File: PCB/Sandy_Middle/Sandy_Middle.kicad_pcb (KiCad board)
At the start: 2 copper layers, 285 x 73.4 mm, 62 parts, among them J1 Conn_02x02_Top_Bottom, J2 Conn_02x02_Top_Bottom, J3 Conn_02x02_Top_Bottom

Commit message: WIP ネジ穴位置、スイッチ位置調整中
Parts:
- removed EXT_MC7: Conn_01x01, TestPoint:TestPoint_THTPad_D2.0mm_Drill1.0mm
- added H20: MountingHole, locallib:MountingHole_2.2mm_M2_Pad_minimal, F.Cu at (41.3, 13.9)
- added H21: MountingHole, locallib:MountingHole_2.2mm_M2_Pad_minimal, F.Cu at (47.3, 13.9)
- SW_BS1: renamed from SW_BS1.5u1; footprint MX_Alps_Hybrid:MXOnly-1.5U-Hotswap-guide -> MX_Alps_Hybrid:MXOnly-1U-Hotswap-guide
- SW_TAB1: renamed from SW_TAB1.5u1; footprint MX_Alps_Hybrid:MXOnly-1.5U-Hotswap-guide -> MX_Alps_Hybrid:MXOnly-1U-Hotswap-guide
- moved D6 7.24 mm to (287.8, 42.5)
- moved SW_TAB1 4.76 mm to (40.1, 49.6)
- moved SW_BS1 4.76 mm to (287.8, 49.6), turned to 180 degrees
- renumbered SW_R4CenterC1 to SW_R4CNT_C1, SW_R4CenterL1 to SW_R4CNT_L1, SW_R4CenterR1 to SW_R4CNT_R1
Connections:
- D11 pad 1: Mid_row3 -> Mid_row8
- D12 pad 1: Mid_row8 -> Mid_row3
- J2 pad 4: Mid_col7 -> unconnected-(J2-Pin_4-Pad4)_1
- SW_R4CNT_L1 pad 1: Mid_col3 -> Mid_col2
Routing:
- net Mid_row6: track 289.5 -> 0.00 mm, vias 3 -> 0
- net Mid_row1: track 281.4 -> 0.00 mm, vias 3 -> 0
- net Mid_col0: track 201.1 -> 0.00 mm, vias 3 -> 0
- net Mid_col6: track 139.1 -> 0.00 mm, vias 3 -> 0
- net Mid_col3: track 137.7 -> 0.00 mm, vias 3 -> 0
- net Mid_row7: track 131.6 -> 0.00 mm, vias 5 -> 0
- net Mid_row2: track 120.4 -> 0.00 mm, vias 4 -> 0
- net Mid_row3: track 110.2 -> 0.00 mm, vias 1 -> 0
- net Mid_col4: track 94.5 -> 0.00 mm, vias 5 -> 0
- net Mid_row8: track 86.1 -> 0.00 mm, vias 1 -> 0
- net Mid_col2: track 69.1 -> 0.00 mm, vias 2 -> 0
- net Mid_col7: track 40.0 -> 0.00 mm, vias 1 -> 0
- net Net-(D8-A): track 22.1 -> 0.00 mm
- net Net-(D9-A): track 11.4 -> 0.00 mm
- net Net-(D7-A): track 9.12 -> 0.00 mm
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
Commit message: Mid→Topのネジ穴を追加して配置
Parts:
- added ?: , clipboard:1d23b097-72e0-487b-bec7-a328ee8b6ed7, F.Cu at (144.8, -0.45)
- added D1: D, locallib:D_SOD-123_Emphasized_Direction_Line, B.Cu at (41.3, -20.7)
- added D10: D, locallib:D_SOD-123_Emphasized_Direction_Line, B.Cu at (212.8, -19.6)
- added D11: D, locallib:D_SOD-123_Emphasized_Direction_Line, B.Cu at (231.8, -20.7)
- added D12: D, locallib:D_SOD-123_Emphasized_Direction_Line, B.Cu at (250.9, -19.6)
- added D13: D, locallib:D_SOD-123_Emphasized_Direction_Line, B.Cu at (269.9, -20.7)
- added D14: D, locallib:D_SOD-123_Emphasized_Direction_Line, B.Cu at (289.0, -19.6)
- added D16: D, locallib:D_SOD-123_Emphasized_Direction_Line, B.Cu at (141.3, -5.21)
- added D17: D, locallib:D_SOD-123_Emphasized_Direction_Line, B.Cu at (160.4, -5.21)
- added D18: D, locallib:D_SOD-123_Emphasized_Direction_Line, B.Cu at (174.7, -1.64)
- added D19: D, locallib:D_SOD-123_Emphasized_Direction_Line, B.Cu at (179.4, -5.21)
- added D2: D, locallib:D_SOD-123_Emphasized_Direction_Line, B.Cu at (60.4, -19.6)
- added D3: D, locallib:D_SOD-123_Emphasized_Direction_Line, B.Cu at (79.4, -20.7)
- added D4: D, locallib:D_SOD-123_Emphasized_Direction_Line, B.Cu at (98.5, -19.6)
- added D5: D, locallib:D_SOD-123_Emphasized_Direction_Line, B.Cu at (117.5, -20.7)
- added D6: D, locallib:D_SOD-123_Emphasized_Direction_Line, B.Cu at (136.6, -19.6)
- added D7: D, locallib:D_SOD-123_Emphasized_Direction_Line, B.Cu at (193.7, -20.7)
- added D8: D, locallib:D_SOD-123_Emphasized_Direction_Line, B.Cu at (155.6, -20.8)
- added D9: D, locallib:D_SOD-123_Emphasized_Direction_Line, B.Cu at (174.7, -20.7)
- added EXT_TC0: Conn_01x01, TestPoint:TestPoint_THTPad_D2.0mm_Drill1.0mm, B.Cu at (37.8, -30.2)
- added EXT_TC1: Conn_01x01, TestPoint:TestPoint_THTPad_D2.0mm_Drill1.0mm, B.Cu at (75.9, -30.2)
- added EXT_TC2: Conn_01x01, TestPoint:TestPoint_THTPad_D2.0mm_Drill1.0mm, B.Cu at (94.9, -30.2)
- added EXT_TC3: Conn_01x01, TestPoint:TestPoint_THTPad_D2.0mm_Drill1.0mm, B.Cu at (152.1, -30.2)
- added EXT_TC4: Conn_01x01, TestPoint:TestPoint_THTPad_D2.0mm_Drill1.0mm, B.Cu at (171.1, -30.3)
- added EXT_TC5: Conn_01x01, TestPoint:TestPoint_THTPad_D2.0mm_Drill1.0mm, B.Cu at (228.3, -30.2)
- added EXT_TC6: Conn_01x01, TestPoint:TestPoint_THTPad_D2.0mm_Drill1.0mm, B.Cu at (266.4, -30.2)
- added EXT_TR0: Conn_01x01, TestPoint:TestPoint_THTPad_D2.0mm_Drill1.0mm, B.Cu at (42.5, -18.3)
- added EXT_TR1: Conn_01x01, TestPoint:TestPoint_THTPad_D2.0mm_Drill1.0mm, B.Cu at (153.3, -14.7)
- added EXT_TR5: Conn_01x01, TestPoint:TestPoint_THTPad_D2.0mm_Drill1.0mm, B.Cu at (46.1, -18.3)
- added EXT_TR6: Conn_01x01, TestPoint:TestPoint_THTPad_D2.0mm_Drill1.0mm, B.Cu at (149.7, -14.7)
- added H1: MountingHole, locallib:MountingHole_2.2mm_M2_Pad_minimal, B.Cu at (28.2, -30.7)
- added H10: MountingHole, locallib:MountingHole_2.2mm_M2_Pad_minimal, B.Cu at (294.9, -18.3)
- added H11: MountingHole, locallib:MountingHole_2.2mm_M2_Pad_minimal, B.Cu at (142.5, 0.74)
- added H12: MountingHole, locallib:MountingHole_2.2mm_M2_Pad_minimal, B.Cu at (180.6, 0.74)
- added H2: MountingHole, locallib:MountingHole_2.2mm_M2_Pad_minimal, B.Cu at (123.5, -30.7)
- added H3: MountingHole, locallib:MountingHole_2.2mm_M2_Pad_minimal, B.Cu at (199.7, -30.7)
- added H4: MountingHole, locallib:MountingHole_2.2mm_M2_Pad_minimal, B.Cu at (294.9, -30.7)
- added H5: MountingHole, locallib:MountingHole_2.2mm_M2_Pad_minimal, B.Cu at (28.2, -18.3)
- added H6: MountingHole, locallib:MountingHole_2.2mm_M2_Pad_minimal, B.Cu at (66.3, -23.1)
- added H7: MountingHole, locallib:MountingHole_2.2mm_M2_Pad_minimal, B.Cu at (104.4, -23.1)
- added H8: MountingHole, locallib:MountingHole_2.2mm_M2_Pad_minimal, B.Cu at (218.7, -23.1)
- added H9: MountingHole, locallib:MountingHole_2.2mm_M2_Pad_minimal, B.Cu at (256.8, -23.1)
- added H_top_11: MountingHole, locallib:MountingHole_2.2mm_M2_Pad_minimal, B.Cu at (144.9, 55.6)
- added H_top_12: MountingHole, locallib:MountingHole_2.2mm_M2_Pad_minimal, B.Cu at (183.0, 55.6)
- added J1: Conn_02x02_Top_Bottom, locallib:JST_SH_SM04B-SRSS-TB_1x04-1MP_P1.00mm_Horizontal_wCable_housing_spare_pin, B.Cu at (171.1, -20.7)
- added J2: Conn_02x02_Top_Bottom, locallib:JST_SH_SM04B-SRSS-TB_1x04-1MP_P1.00mm_Horizontal_wCable_housing_spare_pin, B.Cu at (152.1, -20.7)
- added J3: Conn_02x02_Top_Bottom, locallib:JST_SH_SM04B-SRSS-TB_1x04-1MP_P1.00mm_Horizontal_wCable_housing_spare_pin, B.Cu at (135.4, -18.3)
- added REF**: 60_Outline, locallib:60_Outline-Sandy-Top2, F.Cu at (161.6, -14.7)
- added SW_-1: SW_Push, MX_Alps_Hybrid:MXOnly-1U-Hotswap-guide, F.Cu at (152.1, -24.3)
- added SW_1: SW_Push, MX_Alps_Hybrid:MXOnly-1U-Hotswap-guide, F.Cu at (56.8, -24.3)
- added SW_10: SW_Push, MX_Alps_Hybrid:MXOnly-1U-Hotswap-guide, F.Cu at (266.4, -24.3)
- added SW_2: SW_Push, MX_Alps_Hybrid:MXOnly-1U-Hotswap-guide, F.Cu at (75.9, -24.3)
- added SW_3: SW_Push, MX_Alps_Hybrid:MXOnly-1U-Hotswap-guide, F.Cu at (94.9, -24.3)
- added SW_4: SW_Push, MX_Alps_Hybrid:MXOnly-1U-Hotswap-screw-hole-side1-guide, F.Cu at (114.0, -24.3)
- added SW_5: SW_Push, MX_Alps_Hybrid:MXOnly-1U-Hotswap-guide, F.Cu at (133.0, -24.3)
- added SW_6: SW_Push, MX_Alps_Hybrid:MXOnly-1U-Hotswap-screw-hole-side1-guide, F.Cu at (190.2, -24.3)
- added SW_7: SW_Push, MX_Alps_Hybrid:MXOnly-1U-Hotswap-guide, F.Cu at (209.2, -24.3)
- added SW_8: SW_Push, MX_Alps_Hybrid:MXOnly-1U-Hotswap-guide, F.Cu at (228.3, -24.3)
- added SW_9: SW_Push, MX_Alps_Hybrid:MXOnly-1U-Hotswap-guide, F.Cu at (247.3, -24.3)
- added SW_=1: SW_Push, MX_Alps_Hybrid:MXOnly-1U-Hotswap-guide, F.Cu at (171.0, -24.3)
- added SW_ESC1: SW_Push, MX_Alps_Hybrid:MXOnly-1U-Hotswap-guide, F.Cu at (37.8, -24.3)
- added SW_INS1: SW_Push, MX_Alps_Hybrid:MXOnly-1U-Hotswap-screw-hole-side1-guide, F.Cu at (285.4, -24.3)
- added SW_T1: SW_Push, MX_Alps_Hybrid:MXOnly-1U-Hotswap-guide, F.Cu at (133.0, -5.21)
- added SW_Y1: SW_Push, MX_Alps_Hybrid:MXOnly-1U-Hotswap-guide, F.Cu at (190.2, -5.21)
- added SW_[1: SW_Push, MX_Alps_Hybrid:MXOnly-1U-Hotswap-guide, F.Cu at (152.1, -5.21)
- added SW_]1: SW_Push, MX_Alps_Hybrid:MXOnly-1U-Hotswap-guide, F.Cu at (171.1, -5.21)
- H_top_10: renamed from H21; moved to B.Cu
- H_top_4: renamed from H20; moved to B.Cu
- moved H_top_4 256.2 mm to (297.3, 24.1)
- moved H_top_10 251.1 mm to (297.3, 36.5), turned to 180 degrees
- moved H_top_7 181.0 mm to (106.8, 31.8)
- moved H_top_6 161.9 mm to (68.7, 31.8)
- moved H_top_8 79.8 mm to (221.1, 31.8)
- moved H_top_9 79.8 mm to (259.2, 31.8)
- moved H_top_5 66.8 mm to (30.6, 36.5)
- moved H_top_1 12.2 mm to (30.6, 24.1), turned to 0 degrees
- moved H_top_3 9.53 mm to (202.0, 24.1)
- moved H_top_2 9.52 mm to (125.8, 24.1)
- renumbered H14 to H_top_1, H12 to H_top_2, H13 to H_top_3, H15 to H_top_5, H16 to H_top_6, H17 to H_top_7, H18 to H_top_8, H19 to H_top_9
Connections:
- H1 pad 1: Mid_GND -> unconnected-(H1-Pad1)
- H10 pad 1: Mid_GND -> unconnected-(H10-Pad1)
- H11 pad 1: Mid_GND -> unconnected-(H11-Pad1)
- H2 pad 1: Mid_GND -> unconnected-(H2-Pad1)
- H3 pad 1: Mid_GND -> unconnected-(H3-Pad1)
- H4 pad 1: Mid_GND -> unconnected-(H4-Pad1)
- H5 pad 1: Mid_GND -> unconnected-(H5-Pad1)
- H6 pad 1: Mid_GND -> unconnected-(H6-Pad1)
- H7 pad 1: Mid_GND -> unconnected-(H7-Pad1)
- H8 pad 1: Mid_GND -> unconnected-(H8-Pad1)
- H9 pad 1: Mid_GND -> unconnected-(H9-Pad1)
- H_top_1 pad 1: Mid_GND -> unconnected-(H_top_1-Pad1)
- H_top_10 pad 1: Mid_GND -> unconnected-(H_top_10-Pad1)
- H_top_2 pad 1: Mid_GND -> unconnected-(H_top_2-Pad1)
- H_top_3 pad 1: Mid_GND -> unconnected-(H_top_3-Pad1)
- H_top_4 pad 1: Mid_GND -> unconnected-(H_top_4-Pad1)
- H_top_5 pad 1: Mid_GND -> unconnected-(H_top_5-Pad1)
- H_top_6 pad 1: Mid_GND -> unconnected-(H_top_6-Pad1)
- H_top_7 pad 1: Mid_GND -> unconnected-(H_top_7-Pad1)
- H_top_8 pad 1: Mid_GND -> unconnected-(H_top_8-Pad1)
- H_top_9 pad 1: Mid_GND -> unconnected-(H_top_9-Pad1)
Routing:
- added copper zone on B.Cu, net unconnected-(H5-Pad1)
- added copper zone on F.Cu, net unconnected-(H5-Pad1)
- removed copper zone on B.Cu, net Mid_GND
- removed copper zone on F.Cu, net Mid_GND
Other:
- board text added: "#Sandy_kbd v.0.2, Top by @jpskenn"
- board text added: "Top 1"
- board text added: "Top 2"
- board text added: "Top 3"
- board text added: "to Mid"

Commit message: Mid→Baseのネジ穴を追加して配置
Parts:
- removed ?: , clipboard:1d23b097-72e0-487b-bec7-a328ee8b6ed7
- removed the D1 at (41.3, -20.7)
- removed the D10 at (212.8, -19.6)
- removed the D11 at (231.8, -20.7)
- removed the D12 at (250.9, -19.6)
- removed the D13 at (269.9, -20.7)
- removed D14, D16, D17, D18, D19: D, locallib:D_SOD-123_Emphasized_Direction_Line
- removed the D2 at (60.4, -19.6)
- removed the D3 at (79.4, -20.7)
- removed the D4 at (98.5, -19.6)
- removed the D5 at (117.5, -20.7)
- removed the D6 at (136.6, -19.6)
- removed the D7 at (193.7, -20.7)
- removed the D8 at (155.6, -20.8)
- removed the D9 at (174.7, -20.7)
- removed EXT_TC0, EXT_TC1, EXT_TC2, EXT_TC3, EXT_TC4, EXT_TC5, EXT_TC6, EXT_TR0, EXT_TR1, EXT_TR5, EXT_TR6: Conn_01x01, TestPoint:TestPoint_THTPad_D2.0mm_Drill1.0mm
- removed the H1 at (28.2, -30.7)
- removed the H11 at (142.5, 0.74)
- removed the H12 at (180.6, 0.74)
- removed the H3 at (199.7, -30.7)
- removed the H4 at (294.9, -30.7)
- removed the H7 at (104.4, -23.1)
- removed the H8 at (218.7, -23.1)
- removed the J1 at (171.1, -20.7)
- removed the J2 at (152.1, -20.7)
- removed the J3 at (135.4, -18.3)
- removed the REF** at (161.6, -14.7)
- removed SW_-1, SW_1, SW_10, SW_2, SW_3, SW_5, SW_7, SW_8, SW_9, SW_=1, SW_ESC1, SW_T1, SW_Y1, SW_[1, SW_]1: SW_Push, MX_Alps_Hybrid:MXOnly-1U-Hotswap-guide
- removed SW_4, SW_6, SW_INS1: SW_Push, MX_Alps_Hybrid:MXOnly-1U-Hotswap-screw-hole-side1-guide
- H10, H2, H5, H6, H9: moved to F.Cu
- moved H6 241.6 mm to (303.2, 24.1)
- moved H5 225.5 mm to (249.7, 24.1)
- moved H9 201.5 mm to (65.1, 39.1), turned to 0 degrees
- moved H8 73.7 mm to (230.6, 36.5), turned to 0 degrees
- moved H2 71.5 mm to (78.2, 24.6), turned to 180 degrees
- moved H10 65.8 mm to (262.8, 39.1), turned to 0 degrees
- moved H4 57.7 mm to (192.5, 24.1), turned to 180 degrees
- moved H3 28.6 mm to (135.4, 24.1)
- moved H7 19.6 mm to (97.3, 36.5)
- renumbered H6 to H11, H7 to H12, H8 to H13, H9 to H14, H10 to H15, H11 to H16, H2 to H7, H5 to H8
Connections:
- H10 pad 1: (no net) -> unconnected-(H10-Pad1)
- H2 pad 1: (no net) -> unconnected-(H2-Pad1)
- H5 pad 1: (no net) -> unconnected-(H5-Pad1)
- H6 pad 1: (no net) -> unconnected-(H6-Pad1)
- H9 pad 1: (no net) -> unconnected-(H9-Pad1)
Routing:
- added copper zone on B.Cu, net unconnected-(H5-Pad1)
- added copper zone on F.Cu, net unconnected-(H5-Pad1)
- removed copper zone on B.Cu, net unconnected-(H8-Pad1)
- removed copper zone on F.Cu, net unconnected-(H8-Pad1)
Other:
- board text added: "Screw to Bottom ↓"
- board text removed: "#Sandy_kbd v.0.2, Top by @jpskenn"
- board text removed: "Top 1"
- board text removed: "Top 2"
- board text removed: "Top 3"
- board text removed: "to Mid"

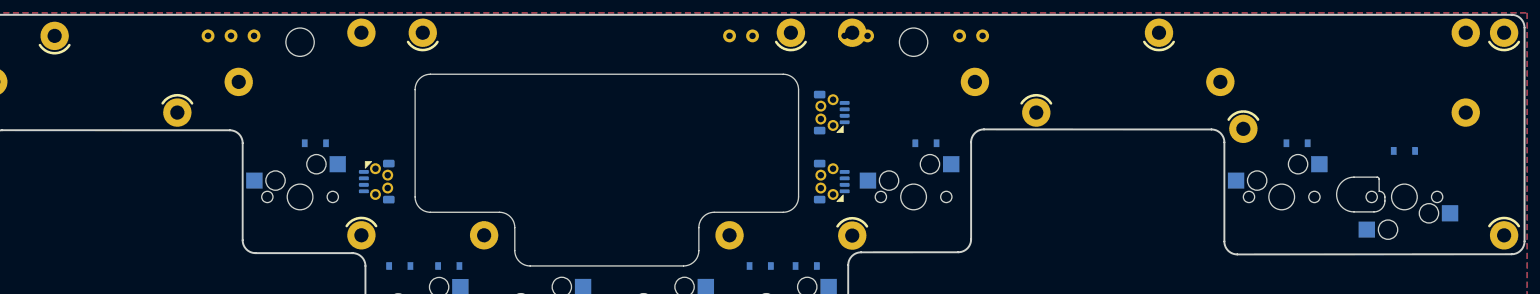
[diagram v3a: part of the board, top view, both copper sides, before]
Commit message: ネジ穴調整、追加
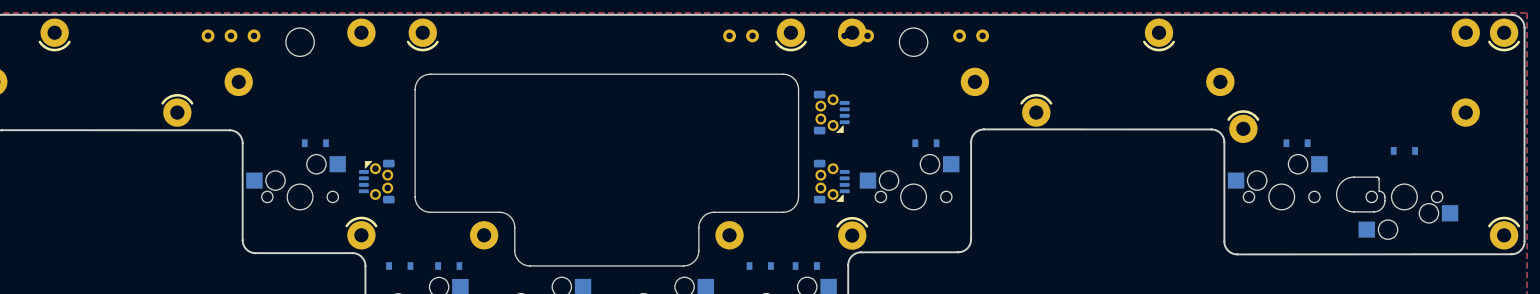
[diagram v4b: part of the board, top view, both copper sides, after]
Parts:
- moved H2 0.49 mm to (78.2, 24.1)
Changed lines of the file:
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@@
 		(allow_soldermask_bridges_in_footprints no)
 		(aux_axis_origin 21.058435 21.05028)
-		(grid_origin 21.058435 21.05028)
+		(grid_origin 24.63031 24.13353)
 		(pcbplotparams
 			(layerselection 0x00310fc_ffffffff)
@@
 		(fp_arc
 			(start 43.375 -18.75004)
-			(mid 44.789228 -18.164256)
+			(mid 44.789192 -18.16425)
 			(end 45.375 -16.75004)
 			(stroke
@@
 		(fp_arc
 			(start 47.375 -12.05004)
-			(mid 45.960801 -12.635829)
+			(mid 45.960765 -12.635823)
 			(end 45.375 -14.05004)
 			(stroke
@@
 		(fp_arc
 			(start 140.475 -18.75004)
-			(mid 141.889228 -18.164256)
+			(mid 141.889192 -18.16425)
 			(end 142.475 -16.75004)
 			(stroke
@@
 		(fp_arc
 			(start 142.475 -2.814254)
-			(mid 141.889168 -1.400099)
+			(mid 141.889174 -1.400064)
 			(end 140.475 -0.814254)
 			(stroke
@@
 		(fp_arc
 			(start 114.175 -9.90004)
-			(mid 114.731482 -11.243546)
+			(mid 114.731476 -11.243582)
 			(end 116.075 -11.80004)
 			(stroke
@@
 		(fp_arc
 			(start 114.923491 -9.898554)
-			(mid 115.274981 -10.74705)
+			(mid 115.274975 -10.747086)
 			(end 116.123491 -11.098554)
 			(stroke
@@
 		(fp_arc
 			(start 116.075 -8.00004)
-			(mid 114.731447 -8.556504)
+			(mid 114.731482 -8.55651)
 			(end 114.175 -9.90004)
 			(stroke
@@
 		(fp_arc
 			(start 116.123491 -8.698554)
-			(mid 115.275017 -9.050062)
+			(mid 115.274982 -9.050056)
 			(end 114.923491 -9.898554)
 			(stroke
@@
 		(fp_arc
 			(start 118.923491 -11.098554)
-			(mid 119.772073 -10.747118)
+			(mid 119.772038 -10.747112)
 			(end 120.123491 -9.898554)
 			(stroke
@@
 		(fp_arc
 			(start 118.975 -11.80004)
-			(mid 120.318452 -11.24351)
+			(mid 120.318488 -11.243516)
 			(end 120.875 -9.90004)
 			(stroke
@@
 		(fp_arc
 			(start 120.123491 -9.898554)
-			(mid 119.772038 -9.049994)
+			(mid 119.772032 -9.050029)
 			(end 118.923491 -8.698554)
 			(stroke
@@
 		(fp_arc
 			(start 120.875 -9.90004)
-			(mid 120.318488 -8.556541)
+			(mid 120.318482 -8.556576)
 			(end 118.975 -8.00004)
 			(stroke
@@
 		(fp_arc
 			(start 14.2875 -4.762415)
-			(mid 14.984924 -6.446239)
+			(mid 14.984924 -6.446243)
 			(end 16.66875 -7.143665)
 			(stroke
@@
 		(fp_arc
 			(start 27.384375 -28.575)
-			(mid 29.068164 -27.87754)
+			(mid 29.068167 -27.877541)
 			(end 29.765625 -26.19375)
 			(stroke
@@
 		(fp_arc
 			(start 27.975 33.570786)
-			(mid 27.389238 34.985022)
+			(mid 27.389238 34.985026)
 			(end 25.975 35.570786)
 			(stroke
@@
 		(fp_arc
 			(start 97.875 -0.60004)
-			(mid 96.460736 -1.185794)
+			(mid 96.460771 -1.1858)
 			(end 95.875 -2.60004)
 			(stroke
@@
 		(fp_arc
 			(start 119.593934 -12.6)
-			(mid 119.806079 -12.512126)
+			(mid 119.806044 -12.51212)
 			(end 119.893934 -12.3)
 			(stroke
@@
 		(fp_arc
 			(start 140.475 -37.80004)
-			(mid 141.889163 -37.214221)
+			(mid 141.889198 -37.214227)
 			(end 142.475 -35.80004)
 			(stroke
@@
 		(fp_arc
 			(start 142.475 -2.628468)
-			(mid 141.889238 -1.21421)
+			(mid 141.889232 -1.214246)
 			(end 140.475 -0.628468)
 			(stroke
@@
 	(footprint "locallib:MountingHole_2.2mm_M2_Pad_minimal"
 		(layer "F.Cu")
-		(at 78.208435 24.622155 180)
+		(at 78.208435 24.13353 180)
 		(descr "Mounting Hole 2.2mm, M2")
 		(tags "mounting hole 2.2mm m2")

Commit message: ネジ穴調整、追加
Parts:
- added ?: , clipboard:1d23b097-72e0-487b-bec7-a328ee8b6ed7, F.Cu at (138.9, -92.1)
- added D1: D, locallib:D_SOD-123_Emphasized_Direction_Line, B.Cu at (31.8, -112.3)
- added D10: D, locallib:D_SOD-123_Emphasized_Direction_Line, B.Cu at (203.2, -112.3)
- added D11: D, locallib:D_SOD-123_Emphasized_Direction_Line, B.Cu at (222.3, -112.3)
- added D12: D, locallib:D_SOD-123_Emphasized_Direction_Line, B.Cu at (241.3, -112.3)
- added D13: D, locallib:D_SOD-123_Emphasized_Direction_Line, B.Cu at (260.4, -112.3)
- added D14: D, locallib:D_SOD-123_Emphasized_Direction_Line, B.Cu at (279.4, -112.3)
- added D16: D, locallib:D_SOD-123_Emphasized_Direction_Line, B.Cu at (127.0, -93.2)
- added D17: D, locallib:D_SOD-123_Emphasized_Direction_Line, B.Cu at (146.1, -93.2)
- added D18: D, locallib:D_SOD-123_Emphasized_Direction_Line, B.Cu at (165.1, -93.2)
- added D19: D, locallib:D_SOD-123_Emphasized_Direction_Line, B.Cu at (184.2, -93.2)
- added D2: D, locallib:D_SOD-123_Emphasized_Direction_Line, B.Cu at (50.8, -112.3)
- added D3: D, locallib:D_SOD-123_Emphasized_Direction_Line, B.Cu at (69.9, -112.3)
- added D4: D, locallib:D_SOD-123_Emphasized_Direction_Line, B.Cu at (88.9, -112.3)
- added D5: D, locallib:D_SOD-123_Emphasized_Direction_Line, B.Cu at (108.0, -112.3)
- added D6: D, locallib:D_SOD-123_Emphasized_Direction_Line, B.Cu at (127.0, -112.3)
- added D7: D, locallib:D_SOD-123_Emphasized_Direction_Line, B.Cu at (146.1, -112.3)
- added D8: D, locallib:D_SOD-123_Emphasized_Direction_Line, B.Cu at (165.1, -112.3)
- added D9: D, locallib:D_SOD-123_Emphasized_Direction_Line, B.Cu at (184.2, -112.3)
- added EXT_TC0: Conn_01x01, TestPoint:TestPoint_THTPad_D2.0mm_Drill1.0mm, B.Cu at (31.8, -121.8)
- added EXT_TC1: Conn_01x01, TestPoint:TestPoint_THTPad_D2.0mm_Drill1.0mm, B.Cu at (69.9, -121.8)
- added EXT_TC2: Conn_01x01, TestPoint:TestPoint_THTPad_D2.0mm_Drill1.0mm, B.Cu at (88.9, -121.8)
- added EXT_TC3: Conn_01x01, TestPoint:TestPoint_THTPad_D2.0mm_Drill1.0mm, B.Cu at (146.1, -121.8)
- added EXT_TC4: Conn_01x01, TestPoint:TestPoint_THTPad_D2.0mm_Drill1.0mm, B.Cu at (165.1, -121.9)
- added EXT_TC5: Conn_01x01, TestPoint:TestPoint_THTPad_D2.0mm_Drill1.0mm, B.Cu at (222.3, -121.8)
- added EXT_TC6: Conn_01x01, TestPoint:TestPoint_THTPad_D2.0mm_Drill1.0mm, B.Cu at (260.4, -121.8)
- added EXT_TR0: Conn_01x01, TestPoint:TestPoint_THTPad_D2.0mm_Drill1.0mm, B.Cu at (27.0, -111.1)
- added EXT_TR1: Conn_01x01, TestPoint:TestPoint_THTPad_D2.0mm_Drill1.0mm, B.Cu at (147.3, -106.3)
- added EXT_TR5: Conn_01x01, TestPoint:TestPoint_THTPad_D2.0mm_Drill1.0mm, B.Cu at (36.5, -111.1)
- added EXT_TR6: Conn_01x01, TestPoint:TestPoint_THTPad_D2.0mm_Drill1.0mm, B.Cu at (143.7, -106.3)
- added H1: MountingHole, locallib:MountingHole_2.2mm_M2_Pad_minimal, F.Cu at (22.2, -122.3)
- added H10: MountingHole, locallib:MountingHole_2.2mm_M2_Pad_minimal, F.Cu at (288.9, -90.9)
- added H11: MountingHole, locallib:MountingHole_2.2mm_M2_Pad_minimal, F.Cu at (136.5, -68.7)
- added H12: MountingHole, locallib:MountingHole_2.2mm_M2_Pad_minimal, F.Cu at (174.6, -68.7)
- added H2: MountingHole, locallib:MountingHole_2.2mm_M2_Pad_minimal, F.Cu at (117.5, -122.3)
- added H3: MountingHole, locallib:MountingHole_2.2mm_M2_Pad_minimal, F.Cu at (193.7, -122.3)
- added H4: MountingHole, locallib:MountingHole_2.2mm_M2_Pad_minimal, F.Cu at (288.9, -122.3)
- added H5: MountingHole, locallib:MountingHole_2.2mm_M2_Pad_minimal, F.Cu at (22.2, -90.9)
- added H6: MountingHole, locallib:MountingHole_2.2mm_M2_Pad_minimal, F.Cu at (60.3, -114.7)
- added H7: MountingHole, locallib:MountingHole_2.2mm_M2_Pad_minimal, F.Cu at (117.5, -90.9)
- added H8: MountingHole, locallib:MountingHole_2.2mm_M2_Pad_minimal, F.Cu at (193.7, -90.9)
- added H9: MountingHole, locallib:MountingHole_2.2mm_M2_Pad_minimal, F.Cu at (250.8, -114.7)
- added J1: Conn_02x02_Top_Bottom, locallib:JST_SH_SM04B-SRSS-TB_1x04-1MP_P1.00mm_Horizontal_wCable_housing_spare_pin, B.Cu at (165.1, -113.3)
- added J2: Conn_02x02_Top_Bottom, locallib:JST_SH_SM04B-SRSS-TB_1x04-1MP_P1.00mm_Horizontal_wCable_housing_spare_pin, B.Cu at (146.1, -113.3)
- added J3: Conn_02x02_Top_Bottom, locallib:JST_SH_SM04B-SRSS-TB_1x04-1MP_P1.00mm_Horizontal_wCable_housing_spare_pin, B.Cu at (129.4, -109.9)
- added REF**: 60_Outline, locallib:60_Outline-Sandy-DN0040-Top, F.Cu at (155.6, -87.3)
- added SW_-1: SW_Push, MX_Alps_Hybrid:MXOnly-1U-Hotswap-screw-hole-side1-guide, F.Cu at (146.1, -115.9)
- added SW_1: SW_Push, MX_Alps_Hybrid:MXOnly-1U-Hotswap-guide, F.Cu at (50.8, -115.9)
- added SW_10: SW_Push, MX_Alps_Hybrid:MXOnly-1U-Hotswap-guide, F.Cu at (260.4, -115.9)
- added SW_2: SW_Push, MX_Alps_Hybrid:MXOnly-1U-Hotswap-guide, F.Cu at (69.9, -115.9)
- added SW_3: SW_Push, MX_Alps_Hybrid:MXOnly-1U-Hotswap-guide, F.Cu at (88.9, -115.9)
- added SW_4: SW_Push, MX_Alps_Hybrid:MXOnly-1U-Hotswap-guide, F.Cu at (108.0, -115.9)
- added SW_5: SW_Push, MX_Alps_Hybrid:MXOnly-1U-Hotswap-screw-hole-side2-guide, F.Cu at (127.0, -115.9)
- added SW_6: SW_Push, MX_Alps_Hybrid:MXOnly-1U-Hotswap-guide, F.Cu at (184.2, -115.9)
- added SW_7: SW_Push, MX_Alps_Hybrid:MXOnly-1U-Hotswap-guide, F.Cu at (203.2, -115.9)
- added SW_8: SW_Push, MX_Alps_Hybrid:MXOnly-1U-Hotswap-screw-hole-side3-guide, F.Cu at (222.3, -115.9)
- added SW_9: SW_Push, MX_Alps_Hybrid:MXOnly-1U-Hotswap-guide, F.Cu at (241.3, -115.9)
- added SW_=1: SW_Push, MX_Alps_Hybrid:MXOnly-1U-Hotswap-guide, F.Cu at (165.1, -115.9)
- added SW_ESC1: SW_Push, MX_Alps_Hybrid:MXOnly-1U-Hotswap-guide, F.Cu at (31.8, -115.9)
- added SW_INS1: SW_Push, MX_Alps_Hybrid:MXOnly-1U-Hotswap-guide, F.Cu at (279.4, -115.9)
- added SW_T1: SW_Push, MX_Alps_Hybrid:MXOnly-1U-Hotswap-guide, F.Cu at (127.0, -96.8)
- added SW_Y1: SW_Push, MX_Alps_Hybrid:MXOnly-1U-Hotswap-guide, F.Cu at (184.2, -96.8)
- added SW_[1: SW_Push, MX_Alps_Hybrid:MXOnly-1U-Hotswap-guide, F.Cu at (146.1, -96.8)
- added SW_]1: SW_Push, MX_Alps_Hybrid:MXOnly-1U-Hotswap-guide, F.Cu at (165.1, -96.8)
- moved H_top_12 19.1 mm to (202.0, 55.6)
- moved H_top_10 19.0 mm to (297.3, 55.6)
- moved H_top_11 19.0 mm to (125.8, 55.6)
- moved H_top_5 19.0 mm to (30.6, 55.6)
- moved H14 9.53 mm to (192.5, 55.6)
- moved H13 9.52 mm to (135.4, 55.6)
- moved H15 5.97 mm to (144.9, 77.7)
- moved H16 5.97 mm to (183.0, 77.7)
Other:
- board size 285 x 73.4 mm -> 285 x 75.2 mm
- board text added: "#Sandy_kbd DN0030, Top & Plate for Mid by @jpskenn"
- board text added: "Top 1"
- board text added: "Top 2"
- board text added: "Top 3"
- board text added: "to Mid"
